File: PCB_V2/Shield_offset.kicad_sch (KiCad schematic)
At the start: 91 parts, among them J1 ADC, J10 I2C, J11 SERVO3, J12 SERVO4, J13 Power OUT, J2 BATT, J3 PWR SW, J4 Screw_Terminal_01x04, J5 SERVO1, J6 ULTRA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

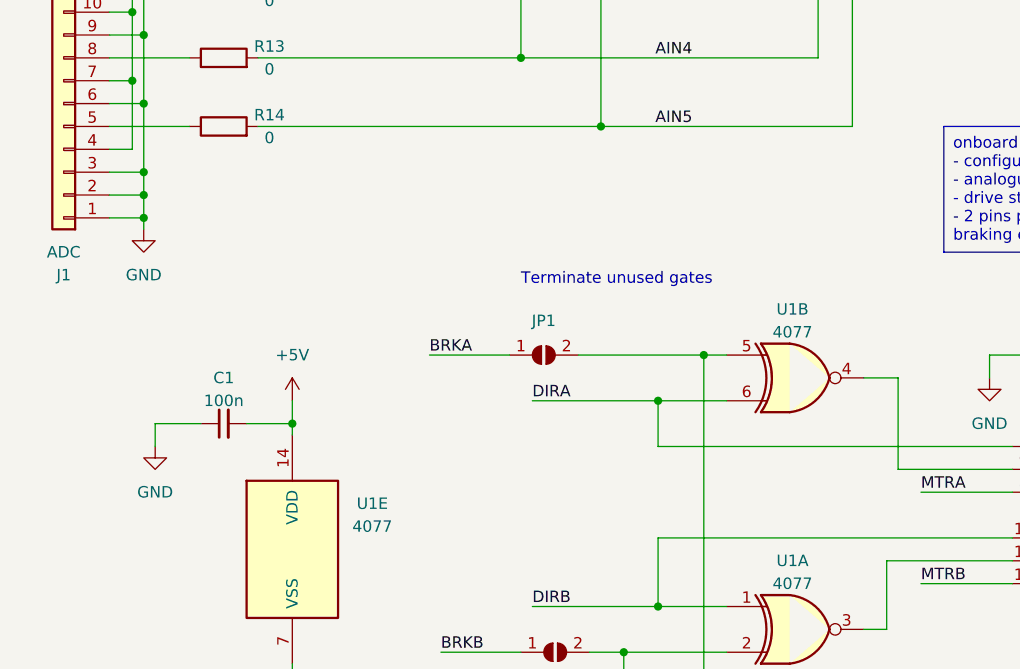
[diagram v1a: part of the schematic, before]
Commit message: Update
Added gnd via's, and caps for LP filter on analog in's
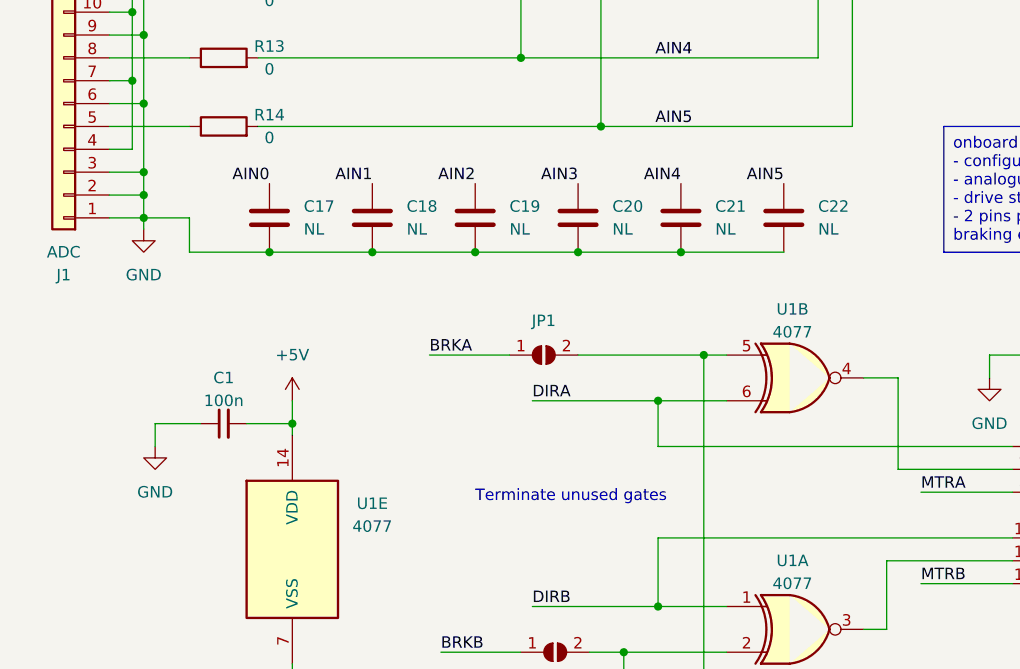
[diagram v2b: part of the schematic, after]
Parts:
- added C17, C18, C19, C20, C21, C22: NL, Capacitor_SMD:C_0805_2012Metric_Pad1.18x1.45mm_HandSolder, symbol Device:C
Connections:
- net AIN0: now also C17.1
- net AIN1: now also C18.1
- net AIN2: now also C19.1
- net AIN3: now also C20.1
- net AIN4: now also C21.1
- net AIN5: now also C22.1
- net GND: now also C17.2, C18.2, C19.2, C20.2, C21.2, C22.2

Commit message: updates
Bug fixes
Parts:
- removed J3: PWR SW, Connector_PinHeader_2.54mm:PinHeader_1x02_P2.54mm_Vertical, symbol Connector:Conn_01x02_Socket
- removed Q3: Q_PMOS_GDS, Package_TO_SOT_SMD:SOT-323_SC-70_Handsoldering, symbol Device:Q_PMOS_GDS
- C4: value C -> 100n
- D1, D11, D12, D13, D14, D15, D16, D2, D3, D5, D6, D7, D8, D9: value D -> SS14
- D21, D4: value D -> US1G
- J4: footprint TerminalBlock:TerminalBlock_bornier-4_P5.08mm -> TerminalBlock_Phoenix:TerminalBlock_Phoenix_MKDS-1,5-4-5.08_1x04_P5.08mm_Horizontal
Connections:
- net +BATT: now also J13.2 (Pin_2)
- net at D4.1 (K), F1.2, Q1.3 (S)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: no longer J13.2 (Pin_2)
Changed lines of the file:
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@@
   (junction (at 54.61 166.37) (diameter 0) (color 0 0 0 0)
   )
-  (junction (at 82.55 59.69) (diameter 0) (color 0 0 0 0)
-  )
   (junction (at 123.19 255.27) (diameter 0) (color 0 0 0 0)
   )
@@
   (junction (at 83.82 247.65) (diameter 0) (color 0 0 0 0)
   )
-  (junction (at 82.55 46.99) (diameter 0) (color 0 0 0 0)
-  )
   (junction (at 72.39 133.35) (diameter 0) (color 0 0 0 0)
   )
@@
     (stroke (width 0) (type default))
   )
-  (wire (pts (xy 87.63 46.99) (xy 82.55 46.99))
-    (stroke (width 0) (type default))
-  )
   (wire (pts (xy 316.23 29.21) (xy 316.23 30.48))
     (stroke (width 0) (type default))
@@
     (stroke (width 0) (type default))
   )
+  (wire (pts (xy 39.37 19.05) (xy 100.33 19.05))
+    (stroke (width 0) (type default))
+  )
   (wire (pts (xy 120.65 31.75) (xy 120.65 34.29))
     (stroke (width 0) (type default))
@@
     (stroke (width 0) (type default))
   )
-  (wire (pts (xy 59.69 19.05) (xy 39.37 19.05))
-    (stroke (width 0) (type default))
-  )
   (wire (pts (xy 161.29 242.57) (xy 161.29 240.03))
     (stroke (width 0) (type default))
@@
     (stroke (width 0) (type default))
   )
-  (wire (pts (xy 82.55 59.69) (xy 82.55 58.42))
-    (stroke (width 0) (type default))
-  )
-  (wire (pts (xy 87.63 54.61) (xy 87.63 59.69))
-    (stroke (width 0) (type default))
-  )
   (wire (pts (xy 196.85 232.41) (xy 232.41 232.41))
     (stroke (width 0) (type default))
@@
     (stroke (width 0) (type default))
   )
-  (wire (pts (xy 87.63 59.69) (xy 82.55 59.69))
-    (stroke (width 0) (type default))
-  )
   (wire (pts (xy 227.33 242.57) (xy 232.41 242.57))
     (stroke (width 0) (type default))
   )
-  (wire (pts (xy 82.55 45.72) (xy 82.55 46.99))
+  (wire (pts (xy 82.55 45.72) (xy 82.55 48.26))
     (stroke (width 0) (type default))
   )
@@
     (stroke (width 0) (type default))
   )
-  (wire (pts (xy 87.63 52.07) (xy 87.63 46.99))
-    (stroke (width 0) (type default))
-  )
   (wire (pts (xy 256.54 54.61) (xy 256.54 63.5))
     (stroke (width 0) (type default))
@@
     (stroke (width 0) (type default))
   )
-  (wire (pts (xy 82.55 59.69) (xy 82.55 60.96))
+  (wire (pts (xy 82.55 58.42) (xy 82.55 60.96))
     (stroke (width 0) (type default))
   )
@@
     (stroke (width 0) (type default))
   )
+  (wire (pts (xy 100.33 19.05) (xy 100.33 33.02))
+    (stroke (width 0) (type default))
+  )
   (wire (pts (xy 95.25 153.67) (xy 152.4 153.67))
     (stroke (width 0) (type default))
@@
     (stroke (width 0) (type default))
   )
-  (wire (pts (xy 82.55 48.26) (xy 82.55 46.99))
-    (stroke (width 0) (type default))
-  )
   (wire (pts (xy 54.61 133.35) (xy 45.72 133.35))
     (stroke (width 0) (type default))
@@
     (stroke (width 0) (type default))
   )
-  (wire (pts (xy 59.69 33.02) (xy 59.69 19.05))
-    (stroke (width 0) (type default))
-  )
   (wire (pts (xy 373.38 163.83) (xy 373.38 165.1))
     (stroke (width 0) (type default))
@@
       (effects (font (size 1.27 1.27)) (justify left))
     )
-    (property "Value" "D" (at 181.61 225.7425 90)
+    (property "Value" "SS14" (at 181.61 225.7425 90)
       (effects (font (size 1.27 1.27)) (justify left))
     )
@@
       (effects (font (size 1.27 1.27)))
     )
-    (property "Value" "D" (at 266.7 25.4 0)
+    (property "Value" "US1G" (at 266.7 25.4 0)
       (effects (font (size 1.27 1.27)))
     )
@@
       (effects (font (size 1.27 1.27)) (justify left))
     )
-    (property "Value" "D" (at 173.99 225.7425 90)
+    (property "Value" "SS14" (at 173.99 225.7425 90)
       (effects (font (size 1.27 1.27)) (justify left))
     )
@@
     )
   )
-  (symbol (lib_id "Device:Q_PMOS_GDS") (at 256.54 31.75 270) (mirror x) (unit 1)
-    (in_bom yes) (on_board yes) (dnp no) (fields_autoplaced)
-    (property "Reference" "Q3" (at 256.54 22.86 90)
-      (effects (font (size 1.27 1.27)))
-    )
-    (property "Value" "Q_PMOS_GDS" (at 256.54 25.4 90)
-      (effects (font (size 1.27 1.27)))
-    )
-    (property "Footprint" "Package_TO_SOT_SMD:SOT-323_SC-70_Handsoldering" (at 259.08 26.67 0)
-      (effects (font (size 1.27 1.27)) hide)
-    )
-    (property "Datasheet" "~" (at 256.54 31.75 0)
-      (effects (font (size 1.27 1.27)) hide)
-    )
-    (pin "1")
-    (pin "2")
-    (pin "3")
-    (instances
-      (project "Shield_offset"
-        (path "/fb5cd38f-308a-430f-ba29-691a649fb154"
-          (reference "Q3") (unit 1)
-        )
-      )
-    )
-  )
   (symbol (lib_id "power:+5V") (at 373.38 97.79 0) (unit 1)
     (in_bom yes) (on_board yes) (dnp no) (fields_autoplaced)
@@
       (effects (font (size 1.27 1.27)) (justify left))
     )
-    (property "Value" "D" (at 83.82 143.1925 90)
+    (property "Value" "SS14" (at 83.82 143.1925 90)
       (effects (font (size 1.27 1.27)) (justify left))
     )
@@
       (effects (font (size 1.27 1.27)) (justify left))
     )
-    (property "Value" "D" (at 181.61 251.1425 90)
+    (property "Value" "SS14" (at 181.61 251.1425 90)
       (effects (font (size 1.27 1.27)) (justify left))
     )
@@
       (effects (font (size 1.27 1.27)) (justify left))
     )
-    (property "Value" "D" (at 48.26 143.1925 90)
+    (property "Value" "SS14" (at 48.26 143.1925 90)
       (effects (font (size 1.27 1.27)) (justify left))
     )
@@
       (effects (font (size 1.27 1.27)) (justify left))
     )
-    (property "Value" "D" (at 173.99 251.1425 90)
+    (property "Value" "SS14" (at 173.99 251.1425 90)
       (effects (font (size 1.27 1.27)) (justify left))
     )
@@
     )
   )
-  (symbol (lib_id "Connector:Conn_01x02_Socket") (at 92.71 54.61 0) (mirror x) (unit 1)
-    (in_bom yes) (on_board yes) (dnp no)
-    (property "Reference" "J3" (at 90.805 55.88 90)
-      (effects (font (size 1.27 1.27)) (justify left))
-    )
-    (property "Value" "PWR SW" (at 93.345 55.88 90)
-      (effects (font (size 1.27 1.27)) (justify left))
-    )
-    (property "Footprint" "Connector_PinHeader_2.54mm:PinHeader_1x02_P2.54mm_Vertical" (at 92.71 54.61 0)
-      (effects (font (size 1.27 1.27)) hide)
-    )
-    (property "Datasheet" "~" (at 92.71 54.61 0)
-      (effects (font (size 1.27 1.27)) hide)
-    )
-    (pin "1")
-    (pin "2")
-    (instances
-      (project "Shield_offset"
-        (path "/fb5cd38f-308a-430f-ba29-691a649fb154"
-          (reference "J3") (unit 1)
-        )
-      )
-    )
-  )
   (symbol (lib_id "Device:D_Schottky") (at 72.39 142.24 270) (unit 1)
     (in_bom yes) (on_board yes) (dnp no) (fields_autoplaced)
@@
       (effects (font (size 1.27 1.27)) (justify left))
     )
-    (property "Value" "D" (at 74.93 143.1925 90)
+    (property "Value" "SS14" (at 74.93 143.1925 90)
       (effects (font (size 1.27 1.27)) (justify left))
     )
@@
       (effects (font (size 1.27 1.27)) (justify left))
     )
-    (property "Footprint" "TerminalBlock:TerminalBlock_bornier-4_P5.08mm" (at 242.57 238.76 0)
+    (property "Footprint" "TerminalBlock_Phoenix:TerminalBlock_Phoenix_MKDS-1,5-4-5.08_1x04_P5.08mm_Horizontal" (at 242.57 238.76 0)
       (effects (font (size 1.27 1.27)) hide)
     )
@@
       (effects (font (size 1.27 1.27)) (justify left))
     )
-    (property "Value" "D" (at 57.15 143.1925 90)
+    (property "Value" "SS14" (at 57.15 143.1925 90)
       (effects (font (size 1.27 1.27)) (justify left))
     )
@@
       (effects (font (size 1.27 1.27)) (justify left))
     )
-    (property "Value" "D" (at 189.23 251.1425 90)
+    (property "Value" "SS14" (at 189.23 251.1425 90)
       (effects (font (size 1.27 1.27)) (justify left))
     )
@@
       (effects (font (size 1.27 1.27)) (justify left))
     )
-    (property "Value" "D" (at 166.37 251.1425 90)
+    (property "Value" "SS14" (at 166.37 251.1425 90)
       (effects (font (size 1.27 1.27)) (justify left))
     )
@@
       (effects (font (size 1.27 1.27)) (justify left))
     )
-    (property "Value" "D" (at 41.91 143.1925 90)
+    (property "Value" "SS14" (at 41.91 143.1925 90)
       (effects (font (size 1.27 1.27)) (justify left))
     )
@@
     )
     (property "Value" "PWR SW" (at 83.82 54.61 90)
-      (effects (font (size 1.27 1.27)) (justify right))
+      (effects (font (size 1.27 1.27)) (justify right) hide)
     )
     (property "Footprint" "Button_Switch_THT:SW_E-Switch_EG2219_DPDT_Angled" (at 82.55 53.34 0)
@@
       (effects (font (size 1.27 1.27)) (justify right))
     )
-    (property "Value" "C" (at 149.86 40.6336 0)
+    (property "Value" "100n" (at 149.86 40.6336 0)
       (effects (font (size 1.27 1.27)) (justify right))
     )
@@
       (effects (font (size 1.27 1.27)) (justify left))
     )
-    (property "Value" "D" (at 166.37 225.7425 90)
+    (property "Value" "SS14" (at 166.37 225.7425 90)
       (effects (font (size 1.27 1.27)) (justify left))
     )
@@
       (effects (font (size 1.27 1.27)) (justify left))
     )
-    (property "Value" "D" (at 66.04 143.1925 90)
+    (property "Value" "SS14" (at 66.04 143.1925 90)
       (effects (font (size 1.27 1.27)) (justify left))
     )
@@
       (effects (font (size 1.27 1.27)) (justify left))
     )
-    (property "Value" "D" (at 189.23 225.7425 90)
+    (property "Value" "SS14" (at 189.23 225.7425 90)
       (effects (font (size 1.27 1.27)) (justify left))
     )
@@
       (effects (font (size 1.27 1.27)) (justify left))
     )
-    (property "Value" "D" (at 62.23 40.64 90)
+    (property "Value" "US1G" (at 62.23 40.64 90)
       (effects (font (size 1.27 1.27)) (justify left))
     )

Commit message: V2 update
Foot prints, component selection, etc.
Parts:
- added Q3: SSM3J356R, Package_TO_SOT_SMD:SOT-23-3, symbol Simulation_SPICE:PMOS
- C2: footprint Capacitor_THT:CP_Radial_D5.0mm_P2.50mm -> Capacitor_SMD:CP_Elec_6.3x7.7; Manuf Part# (none) -> HHXJ350ARA101MF80G
- C5: footprint Capacitor_THT:CP_Radial_D5.0mm_P2.50mm -> Capacitor_SMD:CP_Elec_6.3x5.7
- D1, D2, D3, D5, D6, D7: value SS14 -> CDBW140-G
- D11, D12, D13, D14, D15, D16, D21, D4, D8, D9: footprint Diode_SMD:D_SOD-123 -> Diode_SMD:D_SMA
- U2: value NCP1117-5.0_SOT223 -> MCT1117C-5.0-TP
- U4: footprint Package_TO_SOT_SMD:SOT-23-5 -> Package_TO_SOT_SMD:SOT-353_SC-70-5
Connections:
- net +BATT: now also Q3.2 (S)
- net at D21.2 (A): now also Q3.3 (D)
- net at Q2.6 (D), RN4.4 (R4.1): now also Q3.1 (G)
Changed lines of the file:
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@@
       (effects (font (size 1.27 1.27)) (justify left))
     )
-    (property "Footprint" "Diode_SMD:D_SOD-123" (at 179.07 224.79 0)
+    (property "Footprint" "Diode_SMD:D_SMA" (at 179.07 224.79 0)
       (effects (font (size 1.27 1.27)) hide)
     )
@@
       (effects (font (size 1.27 1.27)))
     )
-    (property "Footprint" "Diode_SMD:D_SOD-123" (at 266.7 29.21 0)
+    (property "Footprint" "Diode_SMD:D_SMA" (at 266.7 29.21 0)
       (effects (font (size 1.27 1.27)) hide)
     )
@@
       (effects (font (size 1.27 1.27)) (justify left))
     )
-    (property "Footprint" "Diode_SMD:D_SOD-123" (at 171.45 224.79 0)
+    (property "Footprint" "Diode_SMD:D_SMA" (at 171.45 224.79 0)
       (effects (font (size 1.27 1.27)) hide)
     )
@@
       (effects (font (size 1.27 1.27)) (justify left))
     )
-    (property "Value" "SS14" (at 83.82 143.1925 90)
+    (property "Value" "CDBW140-G" (at 83.82 143.1925 90)
       (effects (font (size 1.27 1.27)) (justify left))
     )
@@
       (effects (font (size 1.27 1.27)) (justify left))
     )
-    (property "Footprint" "Diode_SMD:D_SOD-123" (at 179.07 250.19 0)
+    (property "Footprint" "Diode_SMD:D_SMA" (at 179.07 250.19 0)
       (effects (font (size 1.27 1.27)) hide)
     )
@@
       (effects (font (size 1.27 1.27)) (justify left))
     )
-    (property "Value" "SS14" (at 48.26 143.1925 90)
+    (property "Value" "CDBW140-G" (at 48.26 143.1925 90)
       (effects (font (size 1.27 1.27)) (justify left))
     )
@@
       (effects (font (size 1.27 1.27)) (justify left))
     )
-    (property "Footprint" "Diode_SMD:D_SOD-123" (at 171.45 250.19 0)
+    (property "Footprint" "Diode_SMD:D_SMA" (at 171.45 250.19 0)
       (effects (font (size 1.27 1.27)) hide)
     )
@@
       (effects (font (size 1.27 1.27)) (justify left))
     )
-    (property "Value" "SS14" (at 74.93 143.1925 90)
+    (property "Value" "CDBW140-G" (at 74.93 143.1925 90)
       (effects (font (size 1.27 1.27)) (justify left))
     )
@@
       (effects (font (size 1.27 1.27)) (justify left))
     )
-    (property "Footprint" "Capacitor_THT:CP_Radial_D5.0mm_P2.50mm" (at 157.48 39.37 0)
+    (property "Footprint" "Capacitor_SMD:CP_Elec_6.3x5.7" (at 157.48 39.37 0)
       (effects (font (size 1.27 1.27)) hide)
     )
@@
     )
   )
+  (symbol (lib_name "PMOS_1") (lib_id "Simulation_SPICE:PMOS") (at 256.54 31.75 270) (mirror x) (unit 1)
+    (in_bom yes) (on_board yes) (dnp no)
+    (property "Reference" "Q3" (at 256.54 24.13 90)
+      (effects (font (size 1.27 1.27)))
+    )
+    (property "Value" "SSM3J356R" (at 256.54 26.67 90)
+      (effects (font (size 1.27 1.27)))
+    )
+    (property "Footprint" "Package_TO_SOT_SMD:SOT-23-3" (at 259.08 26.67 0)
+      (effects (font (size 1.27 1.27)) hide)
+    )
+    (property "Datasheet" "https://ngspice.sourceforge.io/docs/ngspice-manual.pdf" (at 243.84 31.75 0)
+      (effects (font (size 1.27 1.27)) hide)
+    )
+    (property "Sim.Device" "PMOS" (at 239.395 31.75 0)
+      (effects (font (size 1.27 1.27)) hide)
+    )
+    (property "Sim.Type" "VDMOS" (at 237.49 31.75 0)
+      (effects (font (size 1.27 1.27)) hide)
+    )
+    (property "Sim.Pins" "1=D 2=G 3=S" (at 241.3 31.75 0)
+      (effects (font (size 1.27 1.27)) hide)
+    )
+    (pin "1")
+    (pin "2")
+    (pin "3")
+    (instances
+      (project "Shield_offset"
+        (path "/fb5cd38f-308a-430f-ba29-691a649fb154"
+          (reference "Q3") (unit 1)
+        )
+      )
+    )
+  )
   (symbol (lib_id "Device:C_Small") (at 302.26 121.92 90) (unit 1)
     (in_bom yes) (on_board yes) (dnp no) (fields_autoplaced)
@@
       (effects (font (size 1.27 1.27)) hide)
     )
-    (property "Datasheet" "~" (at 247.65 63.5 0)
+    (property "Datasheet" "CFS-0102TB" (at 247.65 63.5 0)
       (effects (font (size 1.27 1.27)) hide)
     )
@@
       (effects (font (size 1.27 1.27)))
     )
-    (property "Footprint" "Package_TO_SOT_SMD:SOT-23-5" (at 217.17 46.99 0)
+    (property "Footprint" "Package_TO_SOT_SMD:SOT-353_SC-70-5" (at 217.17 46.99 0)
       (effects (font (size 1.27 1.27)) hide)
     )
@@
       (effects (font (size 1.27 1.27)) (justify left))
     )
-    (property "Value" "SS14" (at 57.15 143.1925 90)
+    (property "Value" "CDBW140-G" (at 57.15 143.1925 90)
       (effects (font (size 1.27 1.27)) (justify left))
     )
@@
       (effects (font (size 1.27 1.27)) (justify left))
     )
-    (property "Footprint" "Capacitor_THT:CP_Radial_D5.0mm_P2.50mm" (at 100.33 39.37 0)
+    (property "Footprint" "Capacitor_SMD:CP_Elec_6.3x7.7" (at 100.33 39.37 0)
+      (effects (font (size 1.27 1.27)) hide)
+    )
+    (property "Datasheet" "" (at 100.33 39.37 0)
       (effects (font (size 1.27 1.27)) hide)
     )
-    (property "Datasheet" "~" (at 100.33 39.37 0)
+    (property "Manuf Part#" "HHXJ350ARA101MF80G" (at 100.33 39.37 0)
       (effects (font (size 1.27 1.27)) hide)
     )
@@
       (effects (font (size 1.27 1.27)) (justify left))
     )
-    (property "Footprint" "Diode_SMD:D_SOD-123" (at 186.69 250.19 0)
+    (property "Footprint" "Diode_SMD:D_SMA" (at 186.69 250.19 0)
       (effects (font (size 1.27 1.27)) hide)
     )
@@
       (effects (font (size 1.27 1.27)) (justify left))
     )
-    (property "Footprint" "Diode_SMD:D_SOD-123" (at 163.83 250.19 0)
+    (property "Footprint" "Diode_SMD:D_SMA" (at 163.83 250.19 0)
       (effects (font (size 1.27 1.27)) hide)
     )
@@
       (effects (font (size 1.27 1.27)) (justify left))
     )
-    (property "Value" "SS14" (at 41.91 143.1925 90)
+    (property "Value" "CDBW140-G" (at 41.91 143.1925 90)
       (effects (font (size 1.27 1.27)) (justify left))
     )
@@
       (effects (font (size 1.27 1.27)) (justify left))
     )
-    (property "Footprint" "Diode_SMD:D_SOD-123" (at 163.83 224.79 0)
+    (property "Footprint" "Diode_SMD:D_SMA" (at 163.83 224.79 0)
       (effects (font (size 1.27 1.27)) hide)
     )
@@
       (effects (font (size 1.27 1.27)) (justify left))
     )
-    (property "Value" "SS14" (at 66.04 143.1925 90)
+    (property "Value" "CDBW140-G" (at 66.04 143.1925 90)
       (effects (font (size 1.27 1.27)) (justify left))
     )
@@
       (effects (font (size 1.27 1.27)))
     )
-    (property "Value" "NCP1117-5.0_SOT223" (at 137.16 30.48 0)
+    (property "Value" "MCT1117C-5.0-TP" (at 137.16 30.48 0)
       (effects (font (size 1.27 1.27)))
     )
@@
       (effects (font (size 1.27 1.27)) hide)
     )
-    (property "Datasheet" "http://www.onsemi.com/pub_link/Collateral/NCP1117-D.PDF" (at 139.7 40.64 0)
+    (property "Datasheet" "" (at 139.7 40.64 0)
       (effects (font (size 1.27 1.27)) hide)
     )
@@
       (effects (font (size 1.27 1.27)) (justify left))
     )
-    (property "Footprint" "Diode_SMD:D_SOD-123" (at 186.69 224.79 0)
+    (property "Footprint" "Diode_SMD:D_SMA" (at 186.69 224.79 0)
       (effects (font (size 1.27 1.27)) hide)
     )
@@
       (effects (font (size 1.27 1.27)) (justify left))
     )
-    (property "Footprint" "Diode_SMD:D_SOD-123" (at 59.69 39.37 0)
+    (property "Footprint" "Diode_SMD:D_SMA" (at 59.69 39.37 0)
       (effects (font (size 1.27 1.27)) hide)
     )
